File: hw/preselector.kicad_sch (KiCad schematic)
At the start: 50 parts, among them U401 74LVC1G66, U403 MCP23S17_SS, U404 74AHC04, U406 74LVC1G66, U407 74LVC1G66, U408 74LVC1G66, U409 74LVC1G66, U410 74LVC1G66, U411 74LVC1G66, U412 74LVC1G66, U413 74LVC1G66, U414 74LVC1G66, U416 74LVC1G66, U418 74LVC1G3157, U420 PREF7012QDGKR

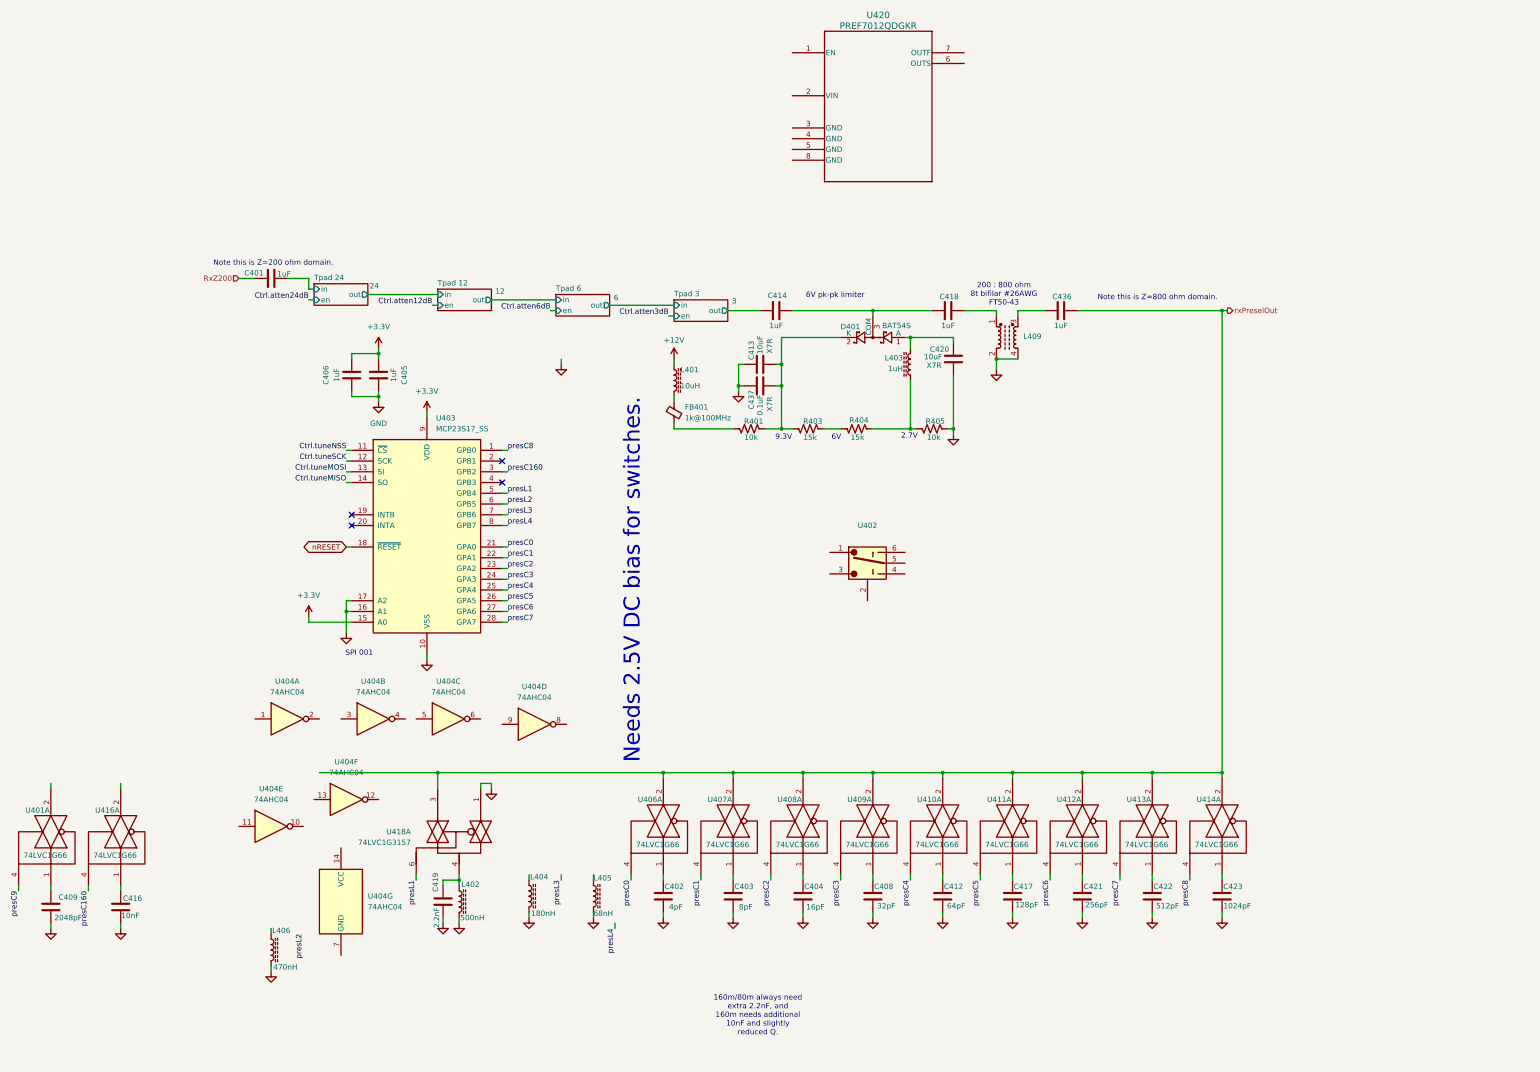
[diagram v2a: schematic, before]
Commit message: "Final" rx preselector design for good digital tuning in 800 ohm domain and general 1MHz..30MHz coverage
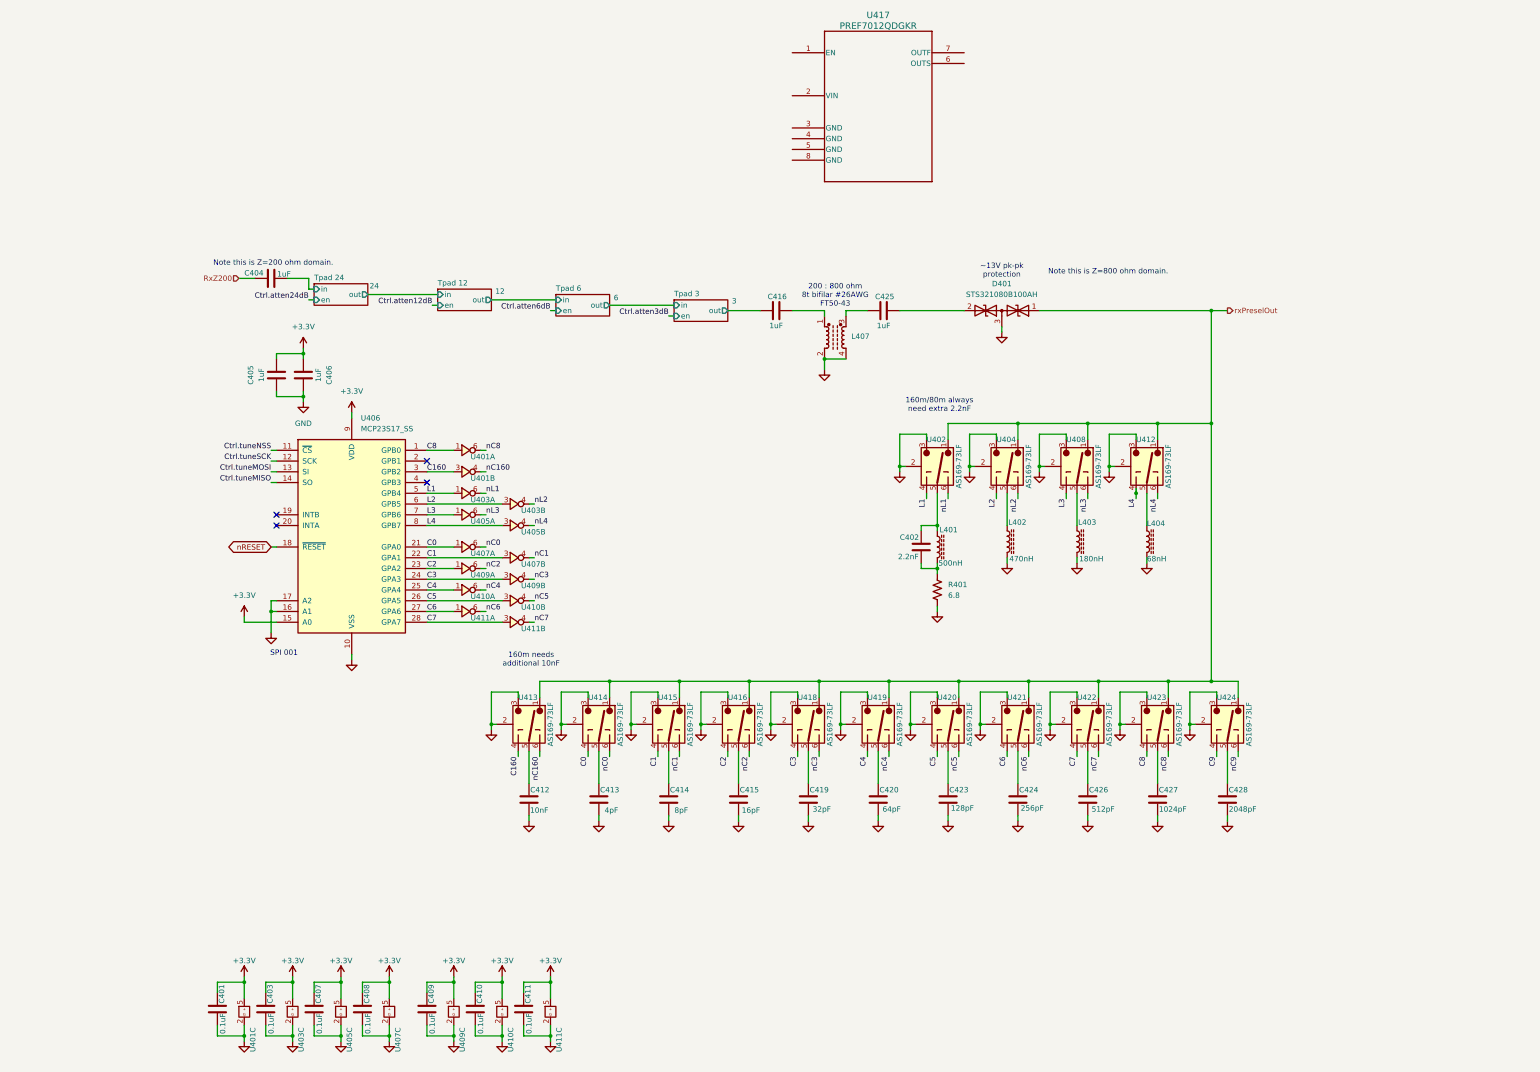
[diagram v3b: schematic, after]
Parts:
- removed C413, C420: 10uF, symbol Device:C
- removed C414, C418: 1uF, symbol Device:C
- removed C437: 0.1uF, symbol Device:C
- removed D401: BAT54S, Package_TO_SOT_SMD:SOT-23, symbol Library:BAT54S
- removed FB401: 1k@100MHz, symbol Device:FerriteBead_Small
- removed L401: 10uH, symbol Device:L_Ferrite
- removed L403: 1uH, symbol Device:L_Ferrite
- removed L406: 470nH, symbol Device:L_Ferrite
- removed R403, R404: 15k, symbol Device:R_US
- removed R405: 10k, symbol Device:R_US
- removed U401, U406, U407, U408, U409, U410, U411, U412, U413, U414, U416: 74LVC1G66, Package_TO_SOT_SMD:SOT-223-5, symbol 74xGxx:74LVC1G66
- removed U402: ~, symbol Library:AS183-92LF
- removed U404: 74AHC04, Package_SO:TSSOP-14_4.4x5mm_P0.65mm, symbol 74xx:74AHC04
- removed U418: 74LVC1G3157, symbol 74xGxx:74LVC1G3157
- added C401, C403, C407, C408, C410, C411: 0.1uF, symbol Device:C
- added C412: 10nF, symbol Device:C
- added C428: 2048pF, symbol Device:C
- added D401: STS321080B100AH, Diode_SMD:D_SOD-323, symbol Diode:SM712_SOT23
- added L402: 470nH, symbol Device:L_Ferrite
- added U401, U403, U405, U407, U409, U410, U411: ~, symbol Library:74LVC2G04
- added U402, U404, U408, U412, U413, U414, U415, U416, U418, U419, U420, U421, U422, U423, U424: AS169-73LF, symbol Library:AS169-73LF
- C409: value 2048pF -> 0.1uF
- C416: value 10nF -> 1uF
- R401: value 10k -> 6.8
- renumbered C419 to C402, C401 to C404, C406 to C405, C405 to C406, C402 to C413, C403 to C414, C404 to C415, C408 to C419, C412 to C420, C417 to C423, C421 to C424, C436 to C425, C422 to C426, C423 to C427, L402 to L401, L404 to L403, L405 to L404, L409 to L407, U403 to U406, U420 to U417
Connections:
- net +3.3V: now also C409.1, C401.1, C403.1, C407.1, C408.1, C410.1, C411.1, U401.5 (V), U403.5 (V), U405.5 (V), U407.5 (V), U409.5 (V), U410.5 (V), U411.5 (V)
- net GND: now also R401.2, C401.2, C403.2, C407.2, C408.2, C410.2, C411.2, C412.2, C428.2, D401.3 (common), L402.2, U401.2 (G), U402.2 (GND), U402.3 (J2), U403.2 (G), U404.2 (GND), U404.3 (J2), U405.2 (G), U407.2 (G), U408.2 (GND), U408.3 (J2), U409.2 (G), U410.2 (G), U411.2 (G), U412.2 (GND), U412.3 (J2), U413.2 (GND), U413.3 (J2), U414.2 (GND), U414.3 (J2), U415.2 (GND), U415.3 (J2), U416.2 (GND), U416.3 (J2), U418.2 (GND), U418.3 (J2), U419.2 (GND), U419.3 (J2), U420.2 (GND), U420.3 (J2), U421.2 (GND), U421.3 (J2), U422.2 (GND), U422.3 (J2), U423.2 (GND), U423.3 (J2), U424.2 (GND), U424.3 (J2); no longer C402.2, C416.2, L401.2
- net Tpad 3/out: now also C416.2
- net rxPreselOut: now also D401.1 (A1), U402.1 (J3), U404.1 (J3), U408.1 (J3), U412.1 (J3), U413.1 (J3), U414.1 (J3), U415.1 (J3), U416.1 (J3), U418.1 (J3), U419.1 (J3), U420.1 (J3), U421.1 (J3), U422.1 (J3), U423.1 (J3), U424.1 (J3); no longer C425.1
- net at C415.1: now also U416.5 (J1)
- net at R401.1: now also C402.2, L401.2
- net at L403.1: now also U408.5 (J1)
- net at C420.1: now also U419.5 (J1)
- net at C402.1, L401.1: now also U402.5 (J1)
- net at C426.1: now also U422.5 (J1)
- net at C416.1: now also L407.1
- net at C423.1: now also U420.5 (J1)
- net at C419.1: now also U418.5 (J1)
- net at C414.1: now also U415.5 (J1)
- net at C413.1: now also U414.5 (J1)
- net at L404.1: now also U412.5 (J1)
- net at C427.1: now also U423.5 (J1)
- net at C424.1: now also U421.5 (J1)
- net presC0 renamed C0
- net C0: now also U407.1, U414.4 (V1)
- net presC1 renamed C1
- net C1: now also U407.3, U415.4 (V1)
- net presC160 renamed C160
- net C160: now also U401.3, U413.4 (V1)
- net presC2 renamed C2
- net C2: now also U409.1, U416.4 (V1)
- net presC3 renamed C3
- net C3: now also U409.3, U418.4 (V1)
- net presC4 renamed C4
- net C4: now also U410.1, U419.4 (V1)
- net presC5 renamed C5
- net C5: now also U410.3, U420.4 (V1)
- net presC6 renamed C6
- net C6: now also U411.1, U421.4 (V1)
- net presC7 renamed C7
- net C7: now also U411.3, U422.4 (V1)
- net presC8 renamed C8
- net C8: now also U401.1, U423.4 (V1)
- net presL1 renamed L1
- net L1: now also U402.4 (V1), U403.1
- net presL2 renamed L2
- net L2: now also U403.3, U404.4 (V1)
- net presL3 renamed L3
- net L3: now also U405.1, U408.4 (V1)
- net presL4 renamed L4
- net L4: now also U405.3, U412.4 (V1)
- new net: L402.1, U404.5 (J1)
- new net: C428.1, U424.5 (J1)
- new net: C412.1, U413.5 (J1)
- new net: C425.1, D401.2 (A2)
- new net C9: U424.4 (V1)
- new net nC0: U407.6, U414.6 (V2)
- new net nC1: U407.4, U415.6 (V2)
- new net nC160: U401.4, U413.6 (V2)
- new net nC2: U409.6, U416.6 (V2)
- new net nC3: U409.4, U418.6 (V2)
- new net nC4: U410.6, U419.6 (V2)
- new net nC5: U410.4, U420.6 (V2)
- new net nC6: U411.6, U421.6 (V2)
- new net nC7: U411.4, U422.6 (V2)
- new net nC8: U401.6, U423.6 (V2)
- new net nC9: U424.6 (V2)
- new net nL1: U402.6 (V2), U403.6
- new net nL2: U403.4, U404.6 (V2)
- new net nL3: U405.6, U408.6 (V2)
- new net nL4: U405.4, U412.6 (V2)
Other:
- note added: "160m needs additional 10nF"
- note added: "160m/80m always need extra 2.2nF"
- note added: "~13V pk-pk protection"
- note removed: "160m/80m always need extra 2.2nF, and 160m needs additional 10nF and slightly reduced Q."
- note removed: "2.7V"
- note removed: "6V"
- note removed: "6V pk-pk limiter"
- note removed: "9.3V"
- note removed: "Needs 2.5V DC bias for switches."
- moved on the sheet: C402, C405, C406, C413, C414, C415, C419, C420, C423, C424, C425, C426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

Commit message: Tx Veer changed to 60V max and reviewed. STM32 now provides Bruene sampling signal to control muxes for QSDs0/1 for fwd/rev complex impedance for tuner and VSWR calculation. Preselector now uses pHEMT switches, as does digital attenuator pad in rx path. Tx/rx relay is now in 200 ohm domain and rx shares most of that with tx for good selectivity and to get benefit of antenna tuner.
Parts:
- removed U417: PREF7012QDGKR, VSSOP8_DGK_TEX, symbol PREF7012QDGKR:PREF7012QDGKR
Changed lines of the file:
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@@
-	)
-	(symbol
-		(lib_id "PREF7012QDGKR:PREF7012QDGKR")
-		(at 151.13 -36.83 0)
-		(unit 1)
-		(exclude_from_sim no)
-		(in_bom yes)
-		(on_board yes)
-		(dnp no)
-		(fields_autoplaced yes)
-		(property "Reference" "U417"
-			(at 171.45 -45.72 0)
-			(effects
-				(font
-					(size 1.524 1.524)
-				)
-			)
-		)
-		(property "Value" "PREF7012QDGKR"
-			(at 171.45 -43.18 0)
-			(effects
-				(font
-					(size 1.524 1.524)
-				)
-			)
-		)
-		(property "Footprint" "VSSOP8_DGK_TEX"
-			(at 151.13 -36.83 0)
-			(effects
-				(font
-					(size 1.27 1.27)
-					(italic yes)
-				)
-				(hide yes)
-			)
-		)
-		(property "Datasheet" "https://www.ti.com/lit/gpn/ref70"
-			(at 151.13 -36.83 0)
-			(effects
-				(font
-					(size 1.27 1.27)
-					(italic yes)
-				)
-				(hide yes)
-			)
-		)
-		(property "Description" ""
-			(at 151.13 -36.83 0)
-			(effects
-				(font
-					(size 1.27 1.27)
-				)
-				(hide yes)
-			)
-		)
-		(pin "1"
-		)
-		(pin "5"
-		)
-		(pin "2"
-		)
-		(pin "4"
-		)
-		(pin "3"
-		)
-		(pin "8"
-		)
-		(pin "7"
-		)
-		(pin "6"
-		)
-		(instances
-			(project ""
-				(path "/8ae46c04-d01a-4756-8774-512b694bfaff/0ee31834-a2c3-474b-9f7c-c9b4f3cadb3f/07084359-e357-43be-bf88-86367e12e534"
-					(reference "U417")
-					(unit 1)
-				)
-			)
-		)
 	)
 	(symbol

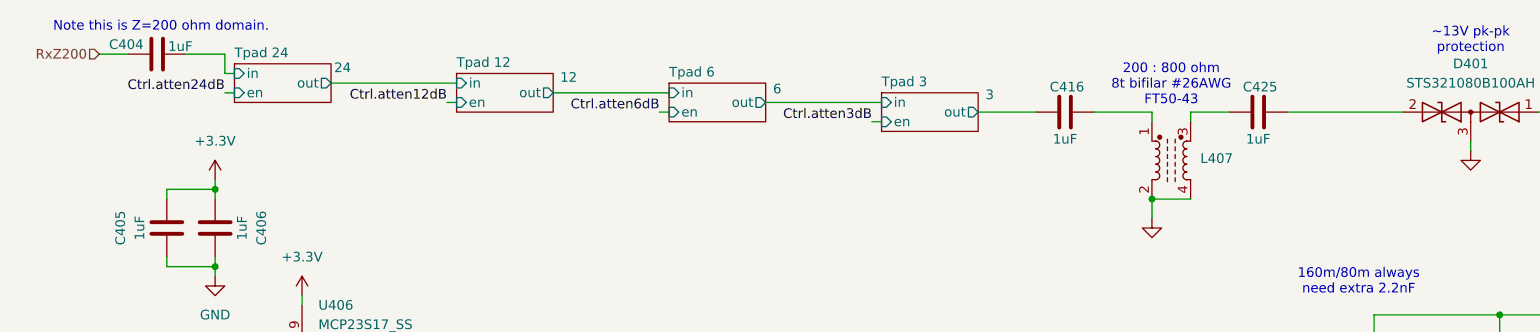
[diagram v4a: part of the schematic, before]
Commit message: Rx arch doc added, some things from it have been incorporated in the schematic as well
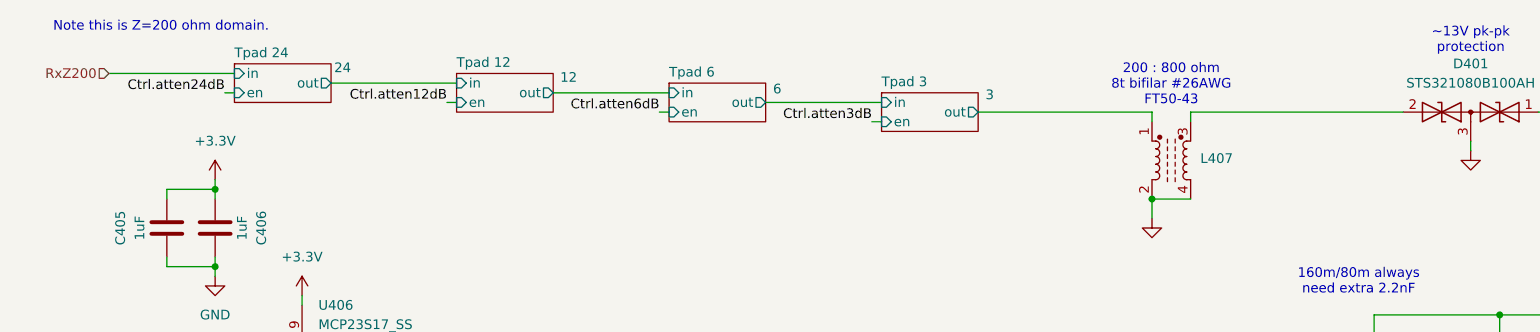
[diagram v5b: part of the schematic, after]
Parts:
- removed C404, C416, C425: 1uF, symbol Device:C
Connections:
- net Tpad 3/out: now also L407.1
- net at L407.3: now also D401.2 (A2)
